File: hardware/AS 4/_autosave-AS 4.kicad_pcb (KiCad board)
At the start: 4 copper layers, 90.5 x 67 mm, 131 parts, among them J1 USB_C_Receptacle_USB2.0_16P, J2 Conn_02x03_Odd_Even, J3 TC2030-NL, Q1 IAUC120N06S5L011, Q2 S8050, Q3 S8050, U1 LM74610QDGKTQ1, U10 BME280, U2 LMR604205SRAKRQ1, U3 TPS2121RUXR, U4 TPS62901Q1, U5 TPS73501DRBR, U6 USBLC6-2SC6, U7 USBLC6-2SC6, U8 CH340C, U9 ESP32-S3-WROOM-1

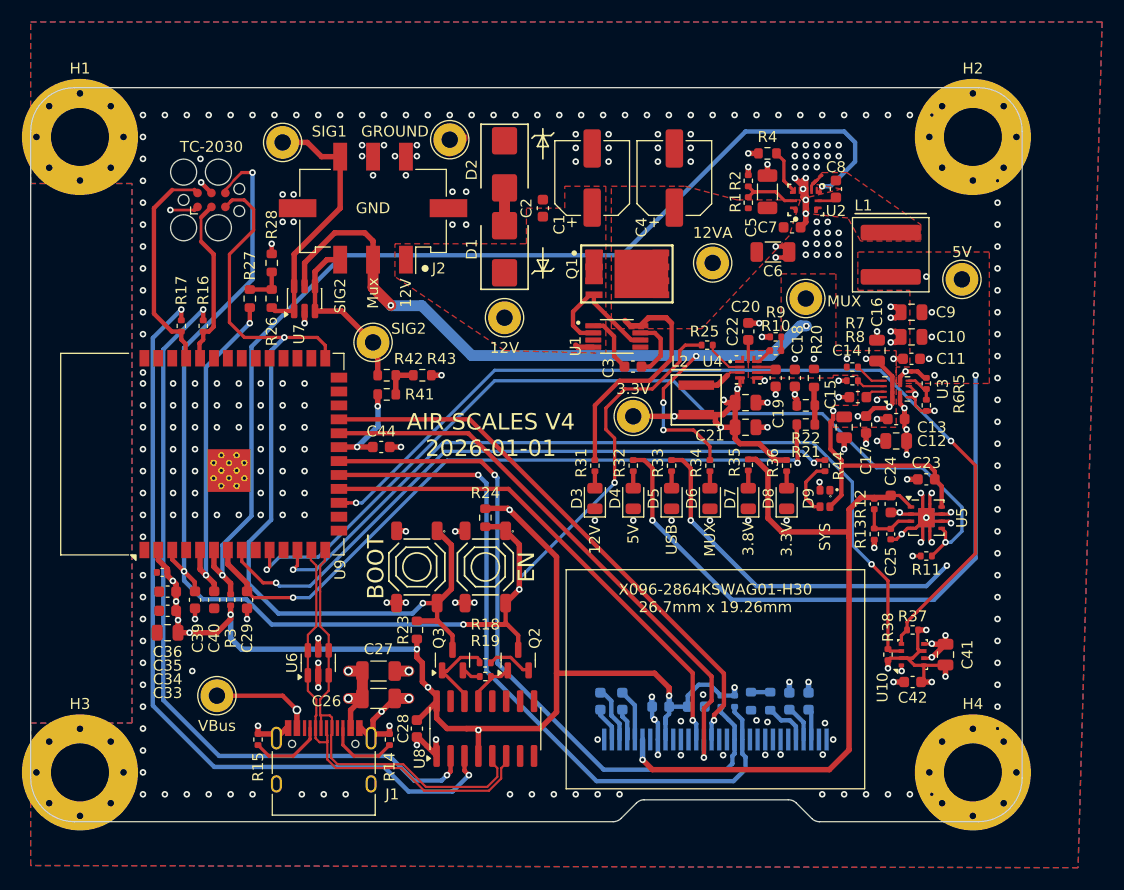
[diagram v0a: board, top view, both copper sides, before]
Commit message: V0.0.9 add OTA and looks stable
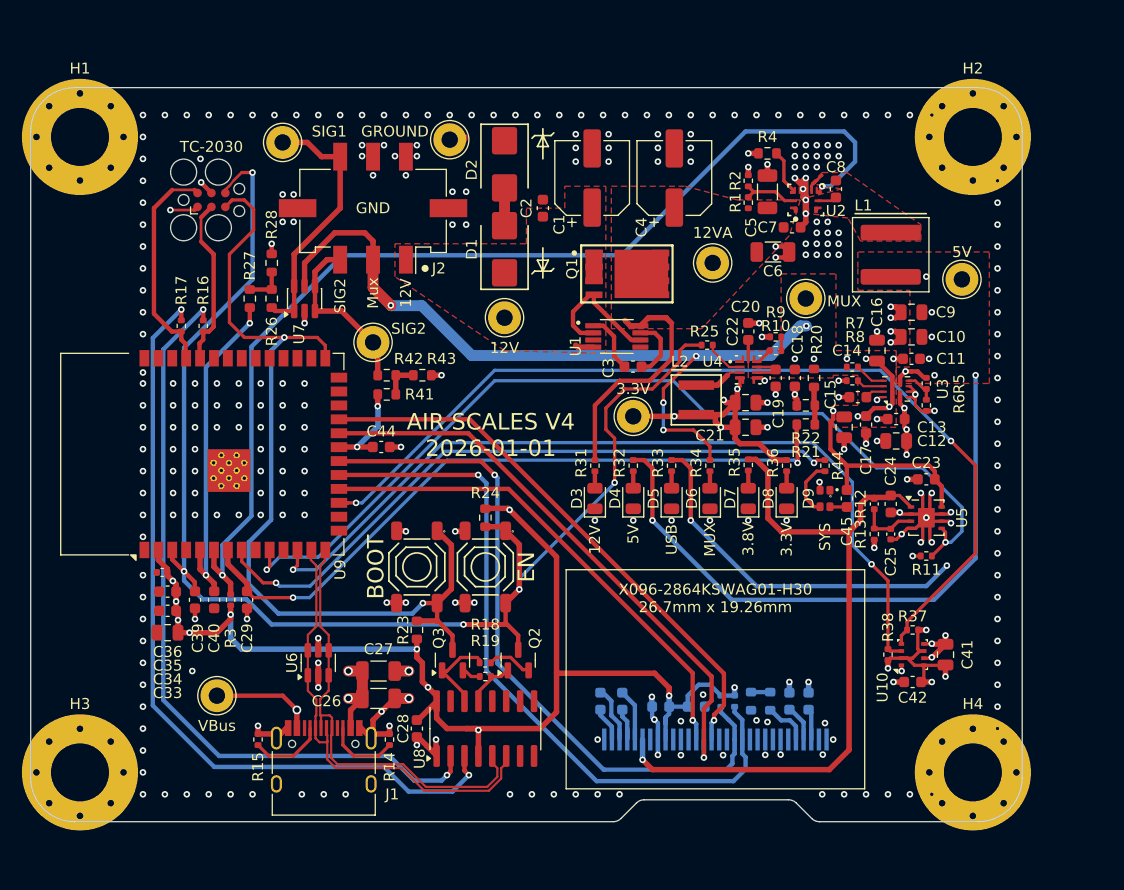
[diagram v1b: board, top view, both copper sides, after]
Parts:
- added C45: 100nF, Capacitor_SMD:C_0603_1608Metric, F.Cu at (268.0, 139.5)
- R44: value 220 -> 500
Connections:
- D9 pad 2: +5VMUX -> Net-(D9-VDD)
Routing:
- net +5VMUX: track 103.9 -> 102.0 mm
- net Net-(D9-VDD): track 0.00 -> 1.56 mm
- net +3.8V: track 65.7 -> 64.8 mm
- removed copper zone on B.Cu, net GND
- removed copper zone on F.Cu, net GND
- removed copper zone on In1.Cu, net GND
